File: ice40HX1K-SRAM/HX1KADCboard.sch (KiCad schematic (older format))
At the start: 0 parts

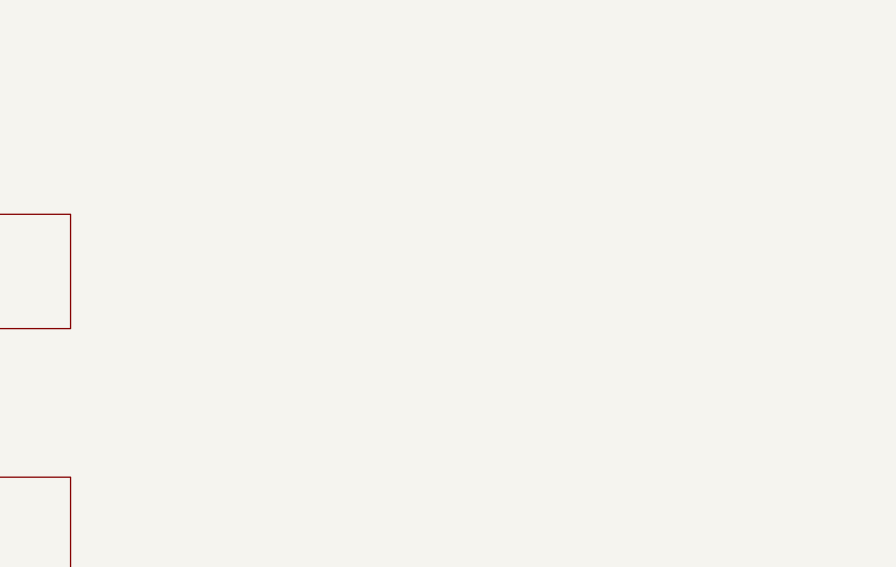
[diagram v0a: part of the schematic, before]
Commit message: add ASE-10.000MHZ XTAL
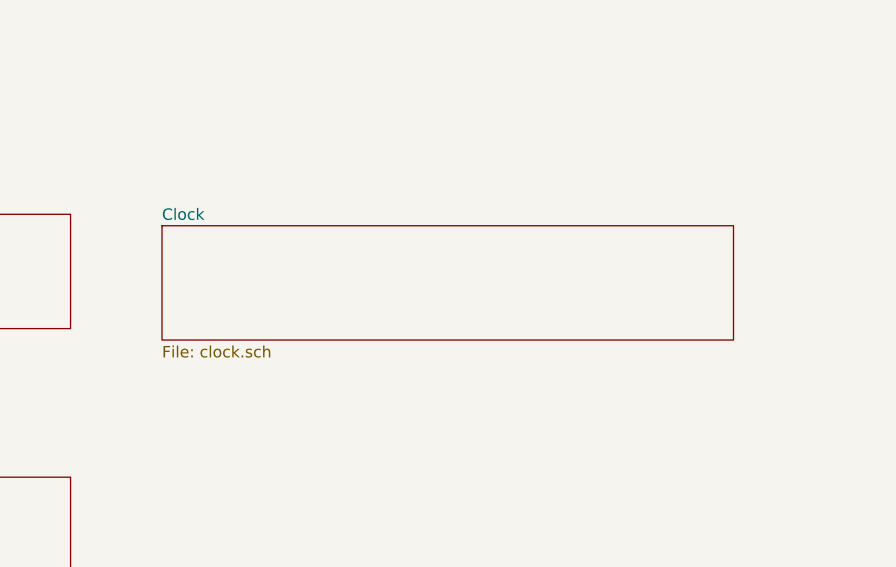
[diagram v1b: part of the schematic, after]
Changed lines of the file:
@@
 $Descr A4 11693 8268
 encoding utf-8
-Sheet 1 8
+Sheet 1 9
 Title ""
 Date ""
@@
 F1 "nrf52.sch" 50
 $EndSheet
+$Sheet
+S 3300 3550 2500 500
+U 5E66F126
+F0 "Clock" 50
+F1 "clock.sch" 50
+$EndSheet
 $EndSCHEMATC
